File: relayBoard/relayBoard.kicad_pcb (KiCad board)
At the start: 4 copper layers, 181.6 x 270.5 mm, 233 parts, among them J1 Conn_01x10, J10 Conn_02x07_Odd_Even, J11 Conn_01x10, J12 Conn_01x10, J13 Conn_01x10, J14 DB50_CON, J2 Conn_01x10, J3 Conn_01x01, J4 Conn_01x01, J5 Conn_01x01, J6 Conn_01x01, J7 Conn_01x01, J8 Conn_01x01, J9 Conn_02x07_Odd_Even, K1 G6S-2, K10 G6S-2, K11 G6S-2, K12 G6S-2, K13 G6S-2, K14 G6S-2, K15 G6S-2, K16 G6S-2, K17 G6S-2, K18 G6S-2, K19 G6S-2, K2 G6S-2, K20 G6S-2, K21 G6S-2, K22 G6S-2, K23 G6S-2, K24 G6S-2, K25 G6S-2, K26 G6S-2, K27 G6S-2, K28 G6S-2, K29 G6S-2, K3 G6S-2, K30 G6S-2, K31 G6S-2, K32 G6S-2, K33 G6S-2, K34 G6S-2, K35 G6S-2, K36 G6S-2, K37 G6S-2, K38 G6S-2, K39 G6S-2, K4 G6S-2, K40 G6S-2, K5 G6S-2, K6 G6S-2, K7 G6S-2, K8 G6S-2, K9 G6S-2, Q1 Q_NMOS_DGS, Q10 Q_NMOS_DGS, Q11 Q_NMOS_DGS, Q12 Q_NMOS_DGS, Q13 Q_NMOS_DGS, Q14 Q_NMOS_DGS, Q15 Q_NMOS_DGS, Q16 Q_NMOS_DGS, Q17 Q_NMOS_DGS, Q18 Q_NMOS_DGS, Q19 Q_NMOS_DGS, Q2 Q_NMOS_DGS, Q20 Q_NMOS_DGS, Q21 Q_NMOS_DGS, Q22 Q_NMOS_DGS, Q23 Q_NMOS_DGS, Q24 Q_NMOS_DGS, Q25 Q_NMOS_DGS, Q26 Q_NMOS_DGS, Q27 Q_NMOS_DGS, Q28 Q_NMOS_DGS, Q29 Q_NMOS_DGS, Q3 Q_NMOS_DGS, Q30 Q_NMOS_DGS, Q31 Q_NMOS_DGS, Q32 Q_NMOS_DGS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

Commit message: First pass layout finished
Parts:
- removed JP1, JP2, JP3: Jumper_3_Bridged12, Connector_PinHeader_2.00mm:PinHeader_1x03_P2.00mm_Vertical
- removed JP4: Jumper_2_Bridged, Connector_PinHeader_2.54mm:PinHeader_1x02_P2.54mm_Vertical
- added C10: C, Resistor_SMD:R_0603_1608Metric, F.Cu at (131.3, 85.0)
- added C11: C, Resistor_SMD:R_0603_1608Metric, F.Cu at (131.3, 75.0)
- added C12: C, Resistor_SMD:R_0603_1608Metric, F.Cu at (131.3, 65.0)
- added C13: C, Resistor_SMD:R_0603_1608Metric, F.Cu at (131.3, 55.0)
- added C14: C, Resistor_SMD:R_0603_1608Metric, F.Cu at (131.3, 45.0)
- added C15: C, Resistor_SMD:R_0603_1608Metric, F.Cu at (131.3, 35.0)
- added C16: C, Resistor_SMD:R_0603_1608Metric, F.Cu at (131.3, 25.0)
- added C17: C, Resistor_SMD:R_0603_1608Metric, F.Cu at (131.3, 15.0)
- added C18: C, Resistor_SMD:R_0603_1608Metric, F.Cu at (131.3, 4.98)
- added C19: C, Resistor_SMD:R_0603_1608Metric, F.Cu at (131.3, -5.02)
- added C20: C, Resistor_SMD:R_0603_1608Metric, F.Cu at (131.3, -15.0)
- added C21: C, Resistor_SMD:R_0603_1608Metric, F.Cu at (131.3, -25.0)
- added C22: C, Resistor_SMD:R_0603_1608Metric, F.Cu at (81.3, 175.0)
- added C23: C, Resistor_SMD:R_0603_1608Metric, F.Cu at (81.3, 165.0)
- added C24: C, Resistor_SMD:R_0603_1608Metric, F.Cu at (81.3, 155.0)
- added C25: C, Resistor_SMD:R_0603_1608Metric, F.Cu at (81.3, 145.0)
- added C26: C, Resistor_SMD:R_0603_1608Metric, F.Cu at (81.3, 135.0)
- added C27: C, Resistor_SMD:R_0603_1608Metric, F.Cu at (81.3, 125.0)
- added C28: C, Resistor_SMD:R_0603_1608Metric, F.Cu at (81.3, 115.0)
- added C29: C, Resistor_SMD:R_0603_1608Metric, F.Cu at (81.3, 105.0)
- added C30: C, Resistor_SMD:R_0603_1608Metric, F.Cu at (81.3, 95.0)
- added C31: C, Resistor_SMD:R_0603_1608Metric, F.Cu at (81.3, 85.0)
- added C32: C, Resistor_SMD:R_0603_1608Metric, F.Cu at (81.3, 75.0)
- added C33: C, Resistor_SMD:R_0603_1608Metric, F.Cu at (81.3, 65.0)
- added C34: C, Resistor_SMD:R_0603_1608Metric, F.Cu at (81.3, 55.0)
- added C35: C, Resistor_SMD:R_0603_1608Metric, F.Cu at (81.3, 45.0)
- added C36: C, Resistor_SMD:R_0603_1608Metric, F.Cu at (81.3, 35.0)
- added C37: C, Resistor_SMD:R_0603_1608Metric, F.Cu at (81.3, 25.0)
- added C38: C, Resistor_SMD:R_0603_1608Metric, F.Cu at (81.3, 15.0)
- added C39: C, Resistor_SMD:R_0603_1608Metric, F.Cu at (81.3, 4.98)
- added C4: C, Resistor_SMD:R_0603_1608Metric, F.Cu at (131.3, 145.0)
- added C40: C, Resistor_SMD:R_0603_1608Metric, F.Cu at (81.3, -5.02)
- added C41: C, Resistor_SMD:R_0603_1608Metric, F.Cu at (81.3, -15.0)
- added C42: C, Resistor_SMD:R_0603_1608Metric, F.Cu at (81.3, -25.0)
- added C43: C, Resistor_SMD:R_0603_1608Metric, F.Cu at (148.8, 70.4)
- added C44: C, Resistor_SMD:R_0603_1608Metric, F.Cu at (95.2, 81.3)
- added C45: C, Resistor_SMD:R_0603_1608Metric, F.Cu at (93.0, 53.8)
- added C46: C, Resistor_SMD:R_0603_1608Metric, F.Cu at (209.8, 144.8)
- added C47: 10u, Resistor_SMD:R_0603_1608Metric, F.Cu at (19.1, 104.1)
- added C48: 10u, Resistor_SMD:R_0603_1608Metric, F.Cu at (26.4, 98.8)
- added C49: C, Resistor_SMD:R_0603_1608Metric, F.Cu at (133.9, -42.2)
- added C5: C, Resistor_SMD:R_0603_1608Metric, F.Cu at (131.3, 135.0)
- added C50: 10u, Resistor_SMD:R_0603_1608Metric, F.Cu at (90.7, -37.1)
- added C51: 1u, Resistor_SMD:R_0603_1608Metric, F.Cu at (95.5, -34.3)
- added C52: 470p, Resistor_SMD:R_0603_1608Metric, F.Cu at (105.9, -45.7)
- added C53: 220u, Resistor_SMD:R_1210_3225Metric, F.Cu at (145.5, -38.6)
- added C6: C, Resistor_SMD:R_0603_1608Metric, F.Cu at (131.3, 125.0)
- added C7: C, Resistor_SMD:R_0603_1608Metric, F.Cu at (131.3, 115.0)
- added C8: C, Resistor_SMD:R_0603_1608Metric, F.Cu at (131.3, 105.0)
- added C9: C, Resistor_SMD:R_0603_1608Metric, F.Cu at (131.3, 95.0)
- added D100: LED, Resistor_SMD:R_0805_2012Metric, F.Cu at (81.1, 59.3)
- added D101: D_Zener, Diode_SMD:D_0805_2012Metric, F.Cu at (76.5, 59.3)
- added D102: D_Zener, Diode_SMD:D_0805_2012Metric, F.Cu at (86.7, 54.5)
- added D103: LED, Resistor_SMD:R_0805_2012Metric, F.Cu at (81.1, 49.3)
- added D104: D_Zener, Diode_SMD:D_0805_2012Metric, F.Cu at (76.5, 49.3)
- added D105: D_Zener, Diode_SMD:D_0805_2012Metric, F.Cu at (86.7, 44.5)
- added D106: LED, Resistor_SMD:R_0805_2012Metric, F.Cu at (81.1, 39.3)
- added D107: D_Zener, Diode_SMD:D_0805_2012Metric, F.Cu at (76.5, 39.3)
- added D108: D_Zener, Diode_SMD:D_0805_2012Metric, F.Cu at (86.7, 34.5)
- added D109: LED, Resistor_SMD:R_0805_2012Metric, F.Cu at (81.1, 29.3)
- added D110: D_Zener, Diode_SMD:D_0805_2012Metric, F.Cu at (76.5, 29.3)
- added D111: D_Zener, Diode_SMD:D_0805_2012Metric, F.Cu at (86.7, 24.5)
- added D112: LED, Resistor_SMD:R_0805_2012Metric, F.Cu at (81.1, 19.3)
- added D113: D_Zener, Diode_SMD:D_0805_2012Metric, F.Cu at (76.5, 19.3)
- added D114: D_Zener, Diode_SMD:D_0805_2012Metric, F.Cu at (86.7, 14.5)
- added D115: LED, Resistor_SMD:R_0805_2012Metric, F.Cu at (81.1, 9.32)
- added D116: D_Zener, Diode_SMD:D_0805_2012Metric, F.Cu at (76.5, 9.32)
- added D117: D_Zener, Diode_SMD:D_0805_2012Metric, F.Cu at (86.7, 4.50)
- added D118: LED, Resistor_SMD:R_0805_2012Metric, F.Cu at (81.1, -0.68)
- added D119: D_Zener, Diode_SMD:D_0805_2012Metric, F.Cu at (76.5, -0.68)
- added D120: D_Zener, Diode_SMD:D_0805_2012Metric, F.Cu at (86.7, -5.50)
- added D121: LED, Resistor_SMD:R_0805_2012Metric, F.Cu at (81.1, -10.7)
- added D122: D_Zener, Diode_SMD:D_0805_2012Metric, F.Cu at (76.5, -10.7)
- added D123: D_Zener, Diode_SMD:D_0805_2012Metric, F.Cu at (86.7, -15.5)
- added D124: LED, Resistor_SMD:R_0805_2012Metric, F.Cu at (81.1, -20.7)
- added D125: D_Zener, Diode_SMD:D_0805_2012Metric, F.Cu at (76.5, -20.7)
- added D126: D_Zener, Diode_SMD:D_0805_2012Metric, F.Cu at (86.7, -25.5)
- added D127: LED, Resistor_SMD:R_0805_2012Metric, F.Cu at (200.4, 176.8)
- added D128: LED, Resistor_SMD:R_0805_2012Metric, F.Cu at (200.4, 166.8)
- added D129: LED, Resistor_SMD:R_0805_2012Metric, F.Cu at (200.4, 156.8)
- added D130: LED, Resistor_SMD:R_0805_2012Metric, F.Cu at (200.4, 146.8)
- added D131: LED, Resistor_SMD:R_0805_2012Metric, F.Cu at (200.4, 136.8)
- added D132: LED, Resistor_SMD:R_0805_2012Metric, F.Cu at (200.4, 126.8)
- added D133: LED, Resistor_SMD:R_0805_2012Metric, F.Cu at (200.4, 116.8)
- added D134: LED, Resistor_SMD:R_0805_2012Metric, F.Cu at (200.4, 106.8)
- added D135: LED, Resistor_SMD:R_0805_2012Metric, F.Cu at (200.4, 96.8)
- added D136: LED, Resistor_SMD:R_0805_2012Metric, F.Cu at (200.4, 86.8)
- added D137: LED, Resistor_SMD:R_0805_2012Metric, F.Cu at (200.4, 76.8)
- added D138: LED, Resistor_SMD:R_0805_2012Metric, F.Cu at (200.4, 66.8)
- added D139: LED, Resistor_SMD:R_0805_2012Metric, F.Cu at (200.4, 56.8)
- added D140: LED, Resistor_SMD:R_0805_2012Metric, F.Cu at (200.4, 46.8)
- added D141: LED, Resistor_SMD:R_0805_2012Metric, F.Cu at (200.4, 36.8)
- added D142: LED, Resistor_SMD:R_0805_2012Metric, F.Cu at (200.4, 26.8)
- added D143: LED, Resistor_SMD:R_0805_2012Metric, F.Cu at (200.4, 16.8)
- added D144: LED, Resistor_SMD:R_0805_2012Metric, F.Cu at (200.4, 6.78)
- added D145: LED, Resistor_SMD:R_0805_2012Metric, F.Cu at (200.4, -3.22)
- added D146: LED, Resistor_SMD:R_0805_2012Metric, F.Cu at (200.4, -13.2)
- added D147: LED, Resistor_SMD:R_0805_2012Metric, F.Cu at (200.4, -23.2)
- added D148: CMZ5934B, Diode_SMD:D_SMA, F.Cu at (96.5, -49.0)
- added D149: DFLS1100, Diode_SMD:D_PowerDI-123, F.Cu at (105.9, -49.0)
- added D150: D, Diode_SMD:D_0805_2012Metric, F.Cu at (149.4, -29.5)
- added D151: PDS360, Diode_SMD:D_PowerDI-5, F.Cu at (130.4, -45.5)
- added D41: D_Zener, Diode_SMD:D_0805_2012Metric, F.Cu at (126.5, 49.3)
- added D42: D_Zener, Diode_SMD:D_0805_2012Metric, F.Cu at (136.7, 44.5)
- added D43: LED, Resistor_SMD:R_0805_2012Metric, F.Cu at (131.1, 39.3)
- added D44: D_Zener, Diode_SMD:D_0805_2012Metric, F.Cu at (126.5, 39.3)
- added D45: D_Zener, Diode_SMD:D_0805_2012Metric, F.Cu at (136.7, 34.5)
- added D46: LED, Resistor_SMD:R_0805_2012Metric, F.Cu at (131.1, 29.3)
- added D47: D_Zener, Diode_SMD:D_0805_2012Metric, F.Cu at (126.5, 29.3)
- added D48: D_Zener, Diode_SMD:D_0805_2012Metric, F.Cu at (136.7, 24.5)
- added D49: LED, Resistor_SMD:R_0805_2012Metric, F.Cu at (131.1, 19.3)
- added D50: D_Zener, Diode_SMD:D_0805_2012Metric, F.Cu at (126.5, 19.3)
- added D51: D_Zener, Diode_SMD:D_0805_2012Metric, F.Cu at (136.7, 14.5)
- added D52: LED, Resistor_SMD:R_0805_2012Metric, F.Cu at (131.1, 9.32)
- added D53: D_Zener, Diode_SMD:D_0805_2012Metric, F.Cu at (126.5, 9.32)
- added D54: D_Zener, Diode_SMD:D_0805_2012Metric, F.Cu at (136.7, 4.50)
- added D55: LED, Resistor_SMD:R_0805_2012Metric, F.Cu at (131.1, -0.68)
- added D56: D_Zener, Diode_SMD:D_0805_2012Metric, F.Cu at (126.5, -0.68)
- added D57: D_Zener, Diode_SMD:D_0805_2012Metric, F.Cu at (136.7, -5.50)
- added D58: LED, Resistor_SMD:R_0805_2012Metric, F.Cu at (131.1, -10.7)
- added D59: D_Zener, Diode_SMD:D_0805_2012Metric, F.Cu at (126.5, -10.7)
- added D60: D_Zener, Diode_SMD:D_0805_2012Metric, F.Cu at (136.7, -15.5)
- added D61: LED, Resistor_SMD:R_0805_2012Metric, F.Cu at (131.1, -20.7)
- added D62: D_Zener, Diode_SMD:D_0805_2012Metric, F.Cu at (126.5, -20.7)
- added D63: D_Zener, Diode_SMD:D_0805_2012Metric, F.Cu at (136.7, -25.5)
- added D64: LED, Resistor_SMD:R_0805_2012Metric, F.Cu at (81.1, 179.3)
- added D65: D_Zener, Diode_SMD:D_0805_2012Metric, F.Cu at (76.5, 179.3)
- added D66: D_Zener, Diode_SMD:D_0805_2012Metric, F.Cu at (86.7, 174.5)
- added D67: LED, Resistor_SMD:R_0805_2012Metric, F.Cu at (81.1, 169.3)
- added D68: D_Zener, Diode_SMD:D_0805_2012Metric, F.Cu at (76.5, 169.3)
- added D69: D_Zener, Diode_SMD:D_0805_2012Metric, F.Cu at (86.7, 164.5)
- added D70: LED, Resistor_SMD:R_0805_2012Metric, F.Cu at (81.1, 159.3)
- added D71: D_Zener, Diode_SMD:D_0805_2012Metric, F.Cu at (76.5, 159.3)
- added D72: D_Zener, Diode_SMD:D_0805_2012Metric, F.Cu at (86.7, 154.5)
- added D73: LED, Resistor_SMD:R_0805_2012Metric, F.Cu at (81.1, 149.3)
- added D74: D_Zener, Diode_SMD:D_0805_2012Metric, F.Cu at (76.5, 149.3)
- added D75: D_Zener, Diode_SMD:D_0805_2012Metric, F.Cu at (86.7, 144.5)
- added D76: LED, Resistor_SMD:R_0805_2012Metric, F.Cu at (81.1, 139.3)
- added D77: D_Zener, Diode_SMD:D_0805_2012Metric, F.Cu at (76.5, 139.3)
- added D78: D_Zener, Diode_SMD:D_0805_2012Metric, F.Cu at (86.7, 134.5)
- added D79: LED, Resistor_SMD:R_0805_2012Metric, F.Cu at (81.1, 129.3)
- added D80: D_Zener, Diode_SMD:D_0805_2012Metric, F.Cu at (76.5, 129.3)
- added D81: D_Zener, Diode_SMD:D_0805_2012Metric, F.Cu at (86.7, 124.5)
- added D82: LED, Resistor_SMD:R_0805_2012Metric, F.Cu at (81.1, 119.3)
- added D83: D_Zener, Diode_SMD:D_0805_2012Metric, F.Cu at (76.5, 119.3)
- added D84: D_Zener, Diode_SMD:D_0805_2012Metric, F.Cu at (86.7, 114.5)
- added D85: LED, Resistor_SMD:R_0805_2012Metric, F.Cu at (81.1, 109.3)
- added D86: D_Zener, Diode_SMD:D_0805_2012Metric, F.Cu at (76.5, 109.3)
- added D87: D_Zener, Diode_SMD:D_0805_2012Metric, F.Cu at (86.7, 104.5)
- added D88: LED, Resistor_SMD:R_0805_2012Metric, F.Cu at (81.1, 99.3)
- added D89: D_Zener, Diode_SMD:D_0805_2012Metric, F.Cu at (76.5, 99.3)
- added D90: D_Zener, Diode_SMD:D_0805_2012Metric, F.Cu at (86.7, 94.5)
- added D91: LED, Resistor_SMD:R_0805_2012Metric, F.Cu at (81.1, 89.3)
- added D92: D_Zener, Diode_SMD:D_0805_2012Metric, F.Cu at (76.5, 89.3)
- added D93: D_Zener, Diode_SMD:D_0805_2012Metric, F.Cu at (86.7, 84.5)
- added D94: LED, Resistor_SMD:R_0805_2012Metric, F.Cu at (81.1, 79.3)
- added D95: D_Zener, Diode_SMD:D_0805_2012Metric, F.Cu at (76.5, 79.3)
- added D96: D_Zener, Diode_SMD:D_0805_2012Metric, F.Cu at (86.7, 74.5)
- added D97: LED, Resistor_SMD:R_0805_2012Metric, F.Cu at (81.1, 69.3)
- added D98: D_Zener, Diode_SMD:D_0805_2012Metric, F.Cu at (76.5, 69.3)
- added D99: D_Zener, Diode_SMD:D_0805_2012Metric, F.Cu at (86.7, 64.5)
- added IC1: ADUM1251, ADUM1251:SO08, F.Cu at (37.6, 155.2)
- added K41: G6S-2, Relay_THT:Relay_DPDT_Omron_G6SK-2, F.Cu at (72.4, -15.0)
- added K42: G6S-2, Relay_THT:Relay_DPDT_Omron_G6SK-2, F.Cu at (72.4, -25.0)
- added K43: CPC1708J, TO381P2016X515X2916-4:TO381P2016X515X2916-4, F.Cu at (172.4, 177.5)
- added K44: CPC1708J, TO381P2016X515X2916-4:TO381P2016X515X2916-4, F.Cu at (172.4, 167.5)
- added K45: CPC1708J, TO381P2016X515X2916-4:TO381P2016X515X2916-4, F.Cu at (172.4, 157.5)
- added K46: CPC1708J, TO381P2016X515X2916-4:TO381P2016X515X2916-4, F.Cu at (172.4, 147.5)
- added K47: CPC1708J, TO381P2016X515X2916-4:TO381P2016X515X2916-4, F.Cu at (172.4, 137.5)
- added K48: CPC1708J, TO381P2016X515X2916-4:TO381P2016X515X2916-4, F.Cu at (172.4, 127.5)
- added K49: CPC1708J, TO381P2016X515X2916-4:TO381P2016X515X2916-4, F.Cu at (172.4, 117.5)
- added K50: CPC1708J, TO381P2016X515X2916-4:TO381P2016X515X2916-4, F.Cu at (172.4, 107.5)
- added K51: CPC1708J, TO381P2016X515X2916-4:TO381P2016X515X2916-4, F.Cu at (172.4, 97.5)
- added K52: CPC1708J, TO381P2016X515X2916-4:TO381P2016X515X2916-4, F.Cu at (172.4, 87.5)
- added K53: CPC1708J, TO381P2016X515X2916-4:TO381P2016X515X2916-4, F.Cu at (172.4, 77.5)
- added K54: CPC1708J, TO381P2016X515X2916-4:TO381P2016X515X2916-4, F.Cu at (172.4, 67.5)
- added K55: CPC1708J, TO381P2016X515X2916-4:TO381P2016X515X2916-4, F.Cu at (172.4, 57.5)
- added K56: CPC1708J, TO381P2016X515X2916-4:TO381P2016X515X2916-4, F.Cu at (172.4, 47.5)
- added K57: CPC1708J, TO381P2016X515X2916-4:TO381P2016X515X2916-4, F.Cu at (172.4, 37.5)
- added K58: CPC1708J, TO381P2016X515X2916-4:TO381P2016X515X2916-4, F.Cu at (172.4, 27.5)
- added K59: CPC1708J, TO381P2016X515X2916-4:TO381P2016X515X2916-4, F.Cu at (172.4, 17.5)
- added K60: CPC1708J, TO381P2016X515X2916-4:TO381P2016X515X2916-4, F.Cu at (172.4, 7.51)
- added K61: CPC1708J, TO381P2016X515X2916-4:TO381P2016X515X2916-4, F.Cu at (172.4, -2.49)
- added K62: CPC1708J, TO381P2016X515X2916-4:TO381P2016X515X2916-4, F.Cu at (172.4, -12.5)
- added K63: CPC1708J, TO381P2016X515X2916-4:TO381P2016X515X2916-4, F.Cu at (172.4, -22.5)
- added Q41: Q_NMOS_DGS, Package_TO_SOT_SMD:SOT-23, F.Cu at (84.1, -11.7)
- added Q42: Q_NMOS_DGS, Package_TO_SOT_SMD:SOT-23, F.Cu at (84.1, -21.7)
- added Q43: Q_NJFET_GSD, Package_TO_SOT_SMD:Infineon_PG-TO-220-7Lead_TabPin8, F.Cu at (160.3, -33.7)
- added R100: 0, Resistor_SMD:R_0603_1608Metric, F.Cu at (76.5, 55.0)
- added R101: 1k, Resistor_SMD:R_0603_1608Metric, F.Cu at (78.3, 55.0)
- added R102: 100, Resistor_SMD:R_0603_1608Metric, F.Cu at (88.2, 58.6)
- added R103: 0, Resistor_SMD:R_0603_1608Metric, F.Cu at (76.5, 45.0)
- added R104: 1k, Resistor_SMD:R_0603_1608Metric, F.Cu at (78.3, 45.0)
- added R105: 100, Resistor_SMD:R_0603_1608Metric, F.Cu at (88.2, 48.6)
- added R106: 0, Resistor_SMD:R_0603_1608Metric, F.Cu at (76.5, 35.0)
- added R107: 1k, Resistor_SMD:R_0603_1608Metric, F.Cu at (78.3, 35.0)
- added R108: 100, Resistor_SMD:R_0603_1608Metric, F.Cu at (88.2, 38.6)
- added R109: 0, Resistor_SMD:R_0603_1608Metric, F.Cu at (76.5, 25.0)
- added R110: 1k, Resistor_SMD:R_0603_1608Metric, F.Cu at (78.3, 25.0)
- added R111: 100, Resistor_SMD:R_0603_1608Metric, F.Cu at (88.2, 28.6)
- added R112: 0, Resistor_SMD:R_0603_1608Metric, F.Cu at (76.5, 15.0)
- added R113: 1k, Resistor_SMD:R_0603_1608Metric, F.Cu at (78.3, 15.0)
- added R114: 100, Resistor_SMD:R_0603_1608Metric, F.Cu at (88.2, 18.6)
- added R115: 0, Resistor_SMD:R_0603_1608Metric, F.Cu at (76.5, 5.01)
- added R116: 1k, Resistor_SMD:R_0603_1608Metric, F.Cu at (78.3, 5.01)
- added R117: 100, Resistor_SMD:R_0603_1608Metric, F.Cu at (88.2, 8.56)
- added R118: 0, Resistor_SMD:R_0603_1608Metric, F.Cu at (76.5, -4.99)
- added R119: 1k, Resistor_SMD:R_0603_1608Metric, F.Cu at (78.3, -4.99)
- added R120: 100, Resistor_SMD:R_0603_1608Metric, F.Cu at (88.2, -1.44)
- added R121: 0, Resistor_SMD:R_0603_1608Metric, F.Cu at (76.5, -15.0)
- added R122: 1k, Resistor_SMD:R_0603_1608Metric, F.Cu at (78.3, -15.0)
- added R123: 100, Resistor_SMD:R_0603_1608Metric, F.Cu at (88.2, -11.4)
- added R124: 0, Resistor_SMD:R_0603_1608Metric, F.Cu at (76.5, -25.0)
- added R125: 1k, Resistor_SMD:R_0603_1608Metric, F.Cu at (78.3, -25.0)
- added R126: 100, Resistor_SMD:R_0603_1608Metric, F.Cu at (88.2, -21.4)
- added R127: 1k, Resistor_SMD:R_0603_1608Metric, F.Cu at (197.4, 176.8)
- added R128: 1k, Resistor_SMD:R_0603_1608Metric, F.Cu at (193.0, 176.8)
- added R129: 1k, Resistor_SMD:R_0603_1608Metric, F.Cu at (197.4, 166.8)
- added R130: 1k, Resistor_SMD:R_0603_1608Metric, F.Cu at (193.0, 166.8)
- added R131: 1k, Resistor_SMD:R_0603_1608Metric, F.Cu at (197.4, 156.8)
- added R132: 1k, Resistor_SMD:R_0603_1608Metric, F.Cu at (193.0, 156.8)
- added R133: 1k, Resistor_SMD:R_0603_1608Metric, F.Cu at (197.4, 146.8)
- added R134: 1k, Resistor_SMD:R_0603_1608Metric, F.Cu at (193.0, 146.8)
- added R135: 1k, Resistor_SMD:R_0603_1608Metric, F.Cu at (197.4, 136.8)
- added R136: 1k, Resistor_SMD:R_0603_1608Metric, F.Cu at (193.0, 136.8)
- added R137: 1k, Resistor_SMD:R_0603_1608Metric, F.Cu at (197.4, 126.8)
- added R138: 1k, Resistor_SMD:R_0603_1608Metric, F.Cu at (193.0, 126.8)
- added R139: 1k, Resistor_SMD:R_0603_1608Metric, F.Cu at (197.4, 116.8)
- added R140: 1k, Resistor_SMD:R_0603_1608Metric, F.Cu at (193.0, 116.8)
- added R141: 1k, Resistor_SMD:R_0603_1608Metric, F.Cu at (197.4, 106.8)
- added R142: 1k, Resistor_SMD:R_0603_1608Metric, F.Cu at (193.0, 106.8)
- added R143: 1k, Resistor_SMD:R_0603_1608Metric, F.Cu at (197.4, 96.8)
- added R144: 1k, Resistor_SMD:R_0603_1608Metric, F.Cu at (193.0, 96.8)
- added R145: 1k, Resistor_SMD:R_0603_1608Metric, F.Cu at (197.4, 86.8)
- added R146: 1k, Resistor_SMD:R_0603_1608Metric, F.Cu at (193.0, 86.8)
- added R147: 1k, Resistor_SMD:R_0603_1608Metric, F.Cu at (197.4, 76.8)
- added R148: 1k, Resistor_SMD:R_0603_1608Metric, F.Cu at (193.0, 76.8)
- added R149: 1k, Resistor_SMD:R_0603_1608Metric, F.Cu at (197.4, 66.8)
- added R150: 1k, Resistor_SMD:R_0603_1608Metric, F.Cu at (193.0, 66.8)
- added R151: 1k, Resistor_SMD:R_0603_1608Metric, F.Cu at (197.4, 56.8)
- added R152: 1k, Resistor_SMD:R_0603_1608Metric, F.Cu at (193.0, 56.8)
- added R153: 1k, Resistor_SMD:R_0603_1608Metric, F.Cu at (197.4, 46.8)
- added R154: 1k, Resistor_SMD:R_0603_1608Metric, F.Cu at (193.0, 46.8)
- added R155: 1k, Resistor_SMD:R_0603_1608Metric, F.Cu at (197.4, 36.8)
- added R156: 1k, Resistor_SMD:R_0603_1608Metric, F.Cu at (193.0, 36.8)
- added R157: 1k, Resistor_SMD:R_0603_1608Metric, F.Cu at (197.4, 26.8)
- added R158: 1k, Resistor_SMD:R_0603_1608Metric, F.Cu at (193.0, 26.8)
- added R159: 1k, Resistor_SMD:R_0603_1608Metric, F.Cu at (197.4, 16.8)
- added R160: 1k, Resistor_SMD:R_0603_1608Metric, F.Cu at (193.0, 16.8)
- added R161: 1k, Resistor_SMD:R_0603_1608Metric, F.Cu at (197.4, 6.78)
- added R162: 1k, Resistor_SMD:R_0603_1608Metric, F.Cu at (193.0, 6.78)
- added R163: 1k, Resistor_SMD:R_0603_1608Metric, F.Cu at (197.4, -3.22)
- added R164: 1k, Resistor_SMD:R_0603_1608Metric, F.Cu at (193.0, -3.22)
- added R165: 1k, Resistor_SMD:R_0603_1608Metric, F.Cu at (197.4, -13.2)
- added R166: 1k, Resistor_SMD:R_0603_1608Metric, F.Cu at (193.0, -13.2)
- added R167: 1k, Resistor_SMD:R_0603_1608Metric, F.Cu at (197.4, -23.2)
- added R168: 1k, Resistor_SMD:R_0603_1608Metric, F.Cu at (193.0, -23.2)
- added R169: R, Resistor_SMD:R_0603_1608Metric, F.Cu at (19.6, 142.5)
- added R170: R, Resistor_SMD:R_0603_1608Metric, F.Cu at (22.6, 142.5)
- added R171: R, Resistor_SMD:R_0603_1608Metric, F.Cu at (49.3, 153.7)
- added R172: R, Resistor_SMD:R_0603_1608Metric, F.Cu at (46.5, 153.7)
- added R173: R, Resistor_SMD:R_0603_1608Metric, F.Cu at (101.6, -42.9)
- added R174: 121k, Resistor_SMD:R_0603_1608Metric, F.Cu at (104.1, -37.8)
- added R175: 10k, Resistor_SMD:R_0603_1608Metric, F.Cu at (99.8, -34.3)
- added R176: 39, Resistor_SMD:R_0603_1608Metric, F.Cu at (105.9, -42.9)
- added R177: R, Resistor_SMD:R_0603_1608Metric, F.Cu at (146.1, -33.8)
- added R178: R, Resistor_SMD:R_0603_1608Metric, F.Cu at (150.4, -33.5)
- added R86: 1k, Resistor_SMD:R_0603_1608Metric, F.Cu at (78.3, 105.0)
- added R87: 100, Resistor_SMD:R_0603_1608Metric, F.Cu at (88.2, 108.6)
- added R88: 0, Resistor_SMD:R_0603_1608Metric, F.Cu at (76.5, 95.0)
- added R89: 1k, Resistor_SMD:R_0603_1608Metric, F.Cu at (78.3, 95.0)
- added R90: 100, Resistor_SMD:R_0603_1608Metric, F.Cu at (88.2, 98.6)
- added R91: 0, Resistor_SMD:R_0603_1608Metric, F.Cu at (76.5, 85.0)
- added R92: 1k, Resistor_SMD:R_0603_1608Metric, F.Cu at (78.3, 85.0)
- added R93: 100, Resistor_SMD:R_0603_1608Metric, F.Cu at (88.2, 88.6)
- added R94: 0, Resistor_SMD:R_0603_1608Metric, F.Cu at (76.5, 75.0)
- added R95: 1k, Resistor_SMD:R_0603_1608Metric, F.Cu at (78.3, 75.0)
- added R96: 100, Resistor_SMD:R_0603_1608Metric, F.Cu at (88.2, 78.6)
- added R97: 0, Resistor_SMD:R_0603_1608Metric, F.Cu at (76.5, 65.0)
- added R98: 1k, Resistor_SMD:R_0603_1608Metric, F.Cu at (78.3, 65.0)
- added R99: 100, Resistor_SMD:R_0603_1608Metric, F.Cu at (88.2, 68.6)
- added T1: 750313457, 750313442:EP10_SMD_H_8PIN_(6052), F.Cu at (118.6, -37.8)
- added U2: PCA9555APW,118, PCA9555APW_118:SOP65P640X110-24N, F.Cu at (98.8, 88.6)
- added U3: PCA9555APW,118, PCA9555APW_118:SOP65P640X110-24N, F.Cu at (98.8, 56.6)
- added U4: PCA9555APW,118, PCA9555APW_118:SOP65P640X110-24N, F.Cu at (214.1, 150.4)
- added U5: LT1117-5.0, Package_TO_SOT_SMD:SOT-223-3_TabPin2, F.Cu at (25.1, 104.9)
- added U6: ADuM4121, Package_SO:SOIC-8_5.23x5.23mm_P1.27mm, F.Cu at (136.7, -38.4)
- added U7: LT8302, Package_SO:SO-8_3.9x4.9mm_P1.27mm, F.Cu at (98.0, -38.4)
- C1, C3: value 1u -> C; footprint Resistor_SMD:R_0603_1608Metric_Pad1.05x0.95mm_HandSolder -> Resistor_SMD:R_0603_1608Metric
- C2: value 1u -> C; footprint Resistor_SMD:R_0603_1608Metric_Pad1.05x0.95mm_HandSolder -> Resistor_SMD:R_0603_1608Metric; moved to F.Cu
- D11, D12, D14, D15, D17, D18, D2, D20, D21, D23, D24, D26, D27, D29, D3, D30, D32, D33, D35, D36, D38, D39, D5, D6, D8, D9: value LED -> D_Zener; footprint Resistor_SMD:R_0805_2012Metric -> Diode_SMD:D_0805_2012Metric
- J1, J2: value Conn_01x10 -> Conn_01x01; footprint Connector_JST:JST_EH_S10B-EH_1x10_P2.50mm_Horizontal -> Connector:Banana_Jack_1Pin
- J10, J9: value Conn_02x07_Odd_Even -> Conn_02x04_Top_Bottom; footprint Connector_PinHeader_2.00mm:PinHeader_2x07_P2.00mm_Vertical -> Connector_Molex:Molex_Micro-Fit_3.0_43045-0800_2x04_P3.00mm_Horizontal
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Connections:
- net /Channel0A/NC renamed /Channel0/NC
- net /Channel10A/NC renamed /sheet5F3D8E21/NC
- net /Channel11A/NC renamed /sheet5F3E9866/NC
- net /Channel12A/NC renamed /sheet5F3E9867/NC
- net /Channel13A/NC renamed /sheet5F3E9868/NC
- net /Channel14A/NC renamed /sheet5F3E9869/NC
- net /Channel15A/NC renamed /sheet5F3E986A/NC
- net /Channel16A/NC renamed /sheet5F3E986B/NC
- net /Channel17A/NC renamed /sheet5F3E986C/NC
- net /Channel18A/NC renamed /sheet5F3E986D/NC
- net /Channel19A/NC renamed /sheet5F3E986E/NC
- net /Channel1A/NC renamed /sheet5F3BDA77/NC
- net /Channel2A/NC renamed /sheet5F3C027D/NC
- net /Channel3A/NC renamed /sheet5F3C2351/NC
- net /Channel4A/NC renamed /sheet5F3C4950/NC
- net /Channel5A/NC renamed /sheet5F3C5DF4/NC
- net /Channel6A/NC renamed /sheet5F3C7669/NC
- net /Channel7A/NC renamed /sheet5F3C9486/NC
- net /Channel8A/NC renamed /sheet5F3CB78B/NC
- net /Channel9A/NC renamed /sheet5F3CDFA2/NC
- C1 pad 1: /5V -> Net-(C1-Pad1)
- C2 pad 1: GND -> Net-(C2-Pad1)
- C2 pad 2: /5V -> GND
- C3 pad 1: +12V -> Net-(C3-Pad1)
- D11 pad 1: Net-(D11-Pad1) -> Net-(C4-Pad1)
- D11 pad 2: Net-(D11-Pad2) -> Net-(D10-Pad1)
- D12 pad 2: Net-(D12-Pad2) -> GND
- D14 pad 1: Net-(D14-Pad1) -> Net-(C5-Pad1)
- D14 pad 2: Net-(D14-Pad2) -> Net-(D13-Pad1)
- D15 pad 2: Net-(D15-Pad2) -> GND
- D17 pad 1: Net-(D17-Pad1) -> Net-(C6-Pad1)
- D17 pad 2: Net-(D17-Pad2) -> Net-(D16-Pad1)
- D18 pad 2: Net-(D18-Pad2) -> GND
- D2 pad 1: Net-(D2-Pad1) -> Net-(C1-Pad1)
- D2 pad 2: Net-(D2-Pad2) -> Net-(D1-Pad1)
- D20 pad 1: Net-(D20-Pad1) -> Net-(C7-Pad1)
- D20 pad 2: Net-(D20-Pad2) -> Net-(D19-Pad1)
- D21 pad 2: Net-(D21-Pad2) -> GND
- D23 pad 1: Net-(D23-Pad1) -> Net-(C8-Pad1)
- D23 pad 2: Net-(D23-Pad2) -> Net-(D22-Pad1)
- D24 pad 2: Net-(D24-Pad2) -> GND
- D26 pad 1: Net-(D26-Pad1) -> Net-(C9-Pad1)
- D26 pad 2: Net-(D26-Pad2) -> Net-(D25-Pad1)
- D27 pad 2: Net-(D27-Pad2) -> GND
- D29 pad 1: Net-(D29-Pad1) -> Net-(C10-Pad1)
- D29 pad 2: Net-(D29-Pad2) -> Net-(D28-Pad1)
- D3 pad 2: Net-(D3-Pad2) -> GND
- D30 pad 2: Net-(D30-Pad2) -> GND
- D32 pad 1: Net-(D32-Pad1) -> Net-(C11-Pad1)
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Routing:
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- added copper zone on F.Cu, net +12V
- added copper zone on In1.Cu, net +12V
- added copper zone on F.Cu, net +5V
- added copper zone on In1.Cu, net +5V
- added copper zone on In2.Cu, net /INPUT_1
- added copper zone on F.Cu, net /INPUT_2
- added copper zone on In2.Cu, net /INPUT_2
- added copper zone on F.Cu, net /INPUT_2_IN
- added copper zone on F.Cu, net GND
- removed copper zone on In2.Cu, net +12V
- removed copper zone on F.Cu, net /5V
- removed copper zone on In2.Cu, net /5V
- removed copper zone on In2.Cu, net /5V_LIN
- removed copper zone on B.Cu, net GND
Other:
- board size 181.6 x 270.5 mm -> 220.7 x 245.6 mm
- board text removed: "12V"
- board text removed: "12V No 5V"
- board text removed: "5V"
- board text removed: "5V/12V"
- board text removed: "A0"
- board text removed: "A1"
- board text removed: "A2"
- board text removed: "Cell Inputs"
- board text removed: "Cells"
- board text removed: "High Voltage"
- board text removed: "Linduino 5V"
- board text removed: "No Power"
- board text removed: "Power"
- board text removed: "Relay Output"
- board text removed: "Relay Outputs"

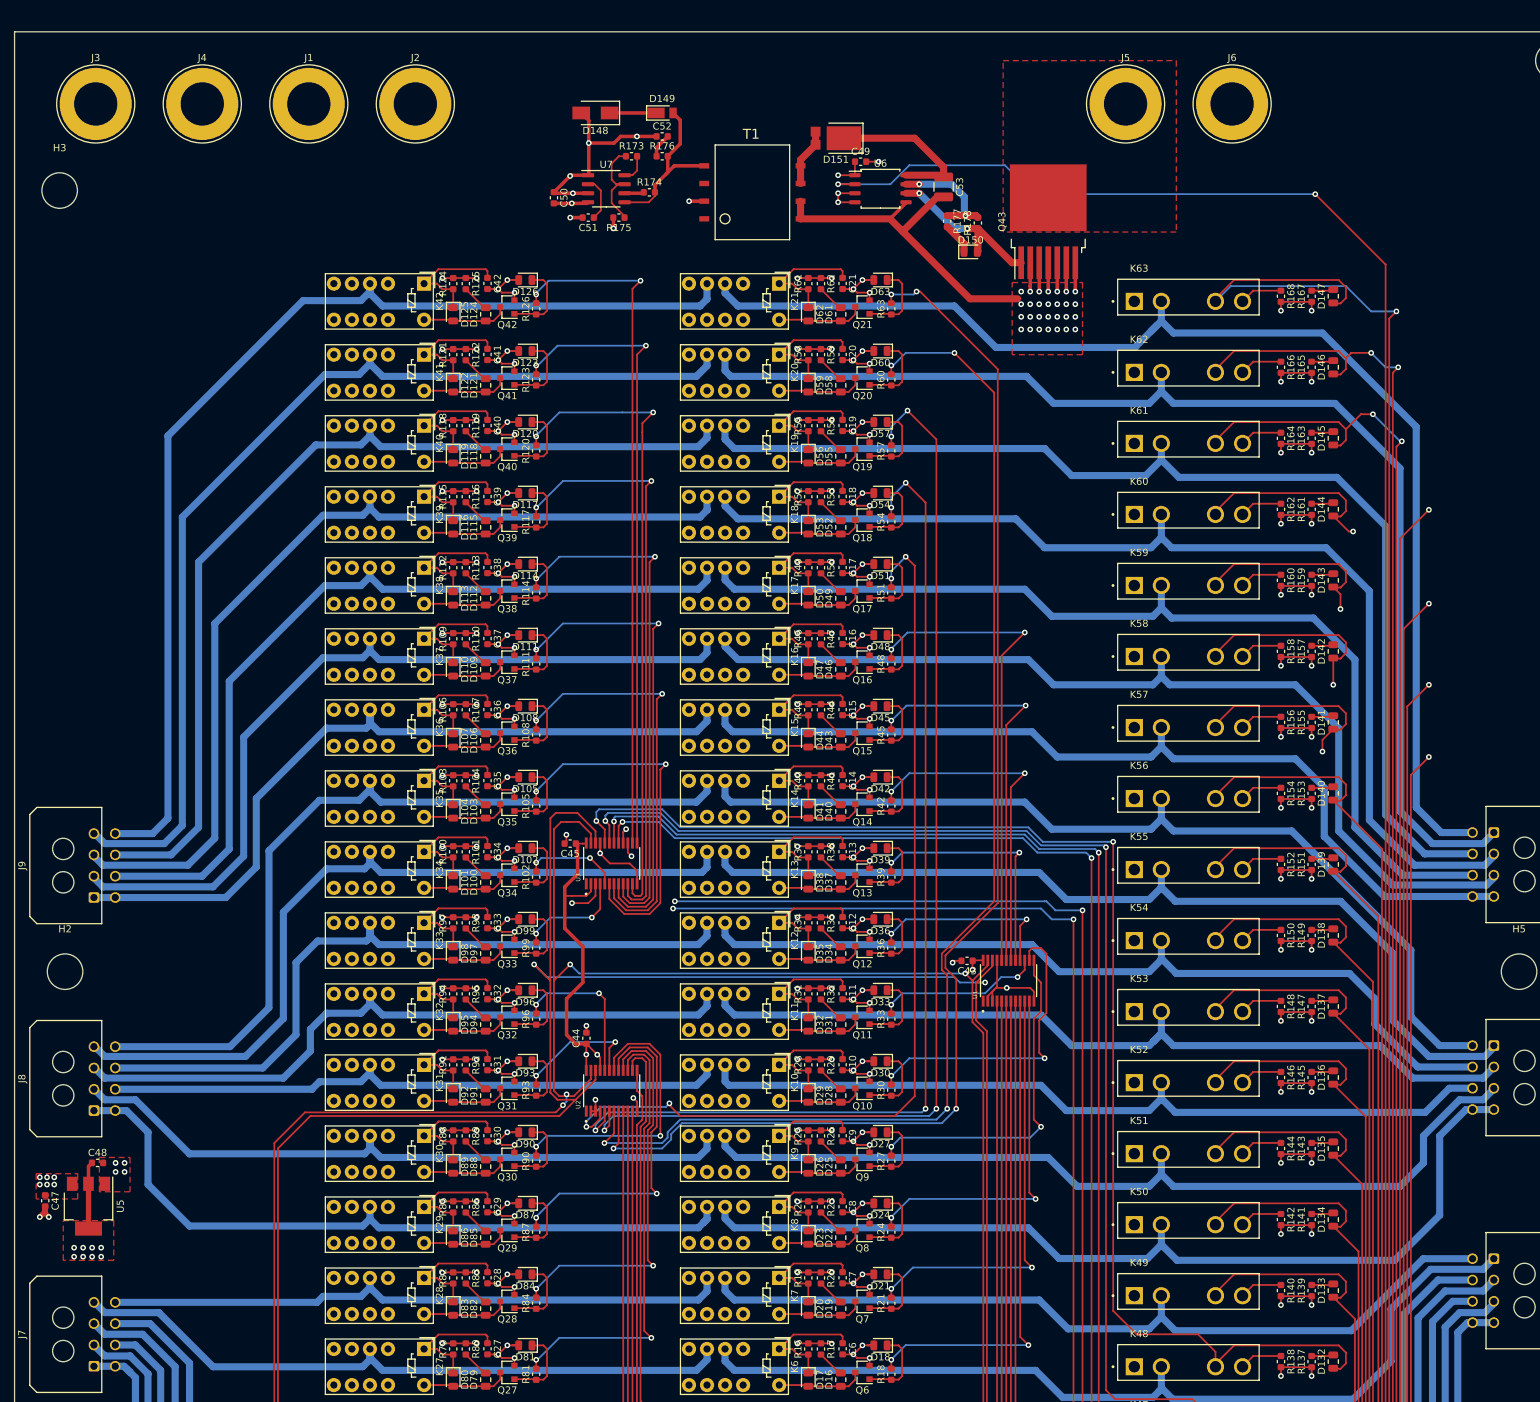
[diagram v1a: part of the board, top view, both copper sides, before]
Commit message: second pass relay board layout
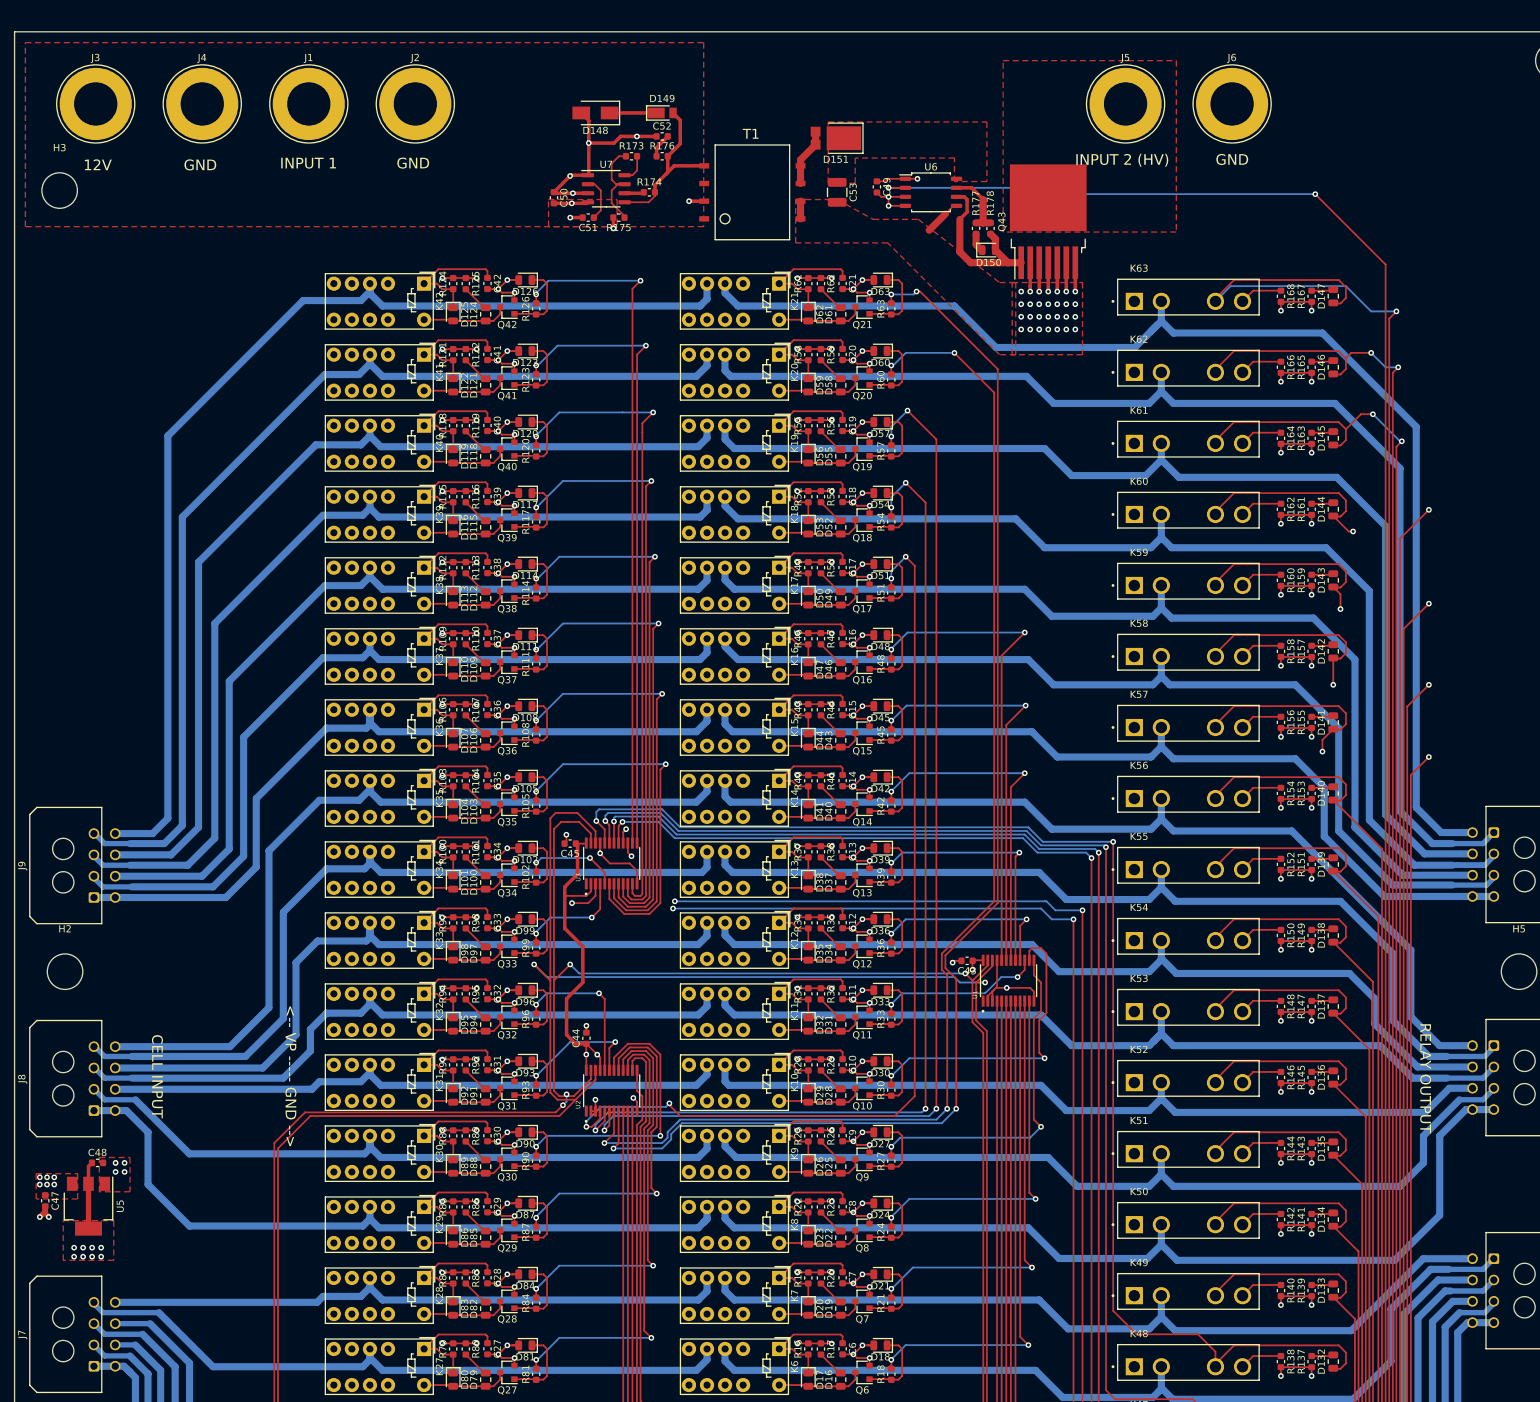
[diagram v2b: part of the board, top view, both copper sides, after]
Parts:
- moved C53 15.0 mm to (130.6, -37.8)
- moved U6 7.13 mm to (143.8, -37.8)
- moved C49 4.23 mm to (136.1, -38.6), turned to 270 degrees
- moved R177 4.19 mm to (150.1, -32.8)
- moved D150 2.55 mm to (151.9, -29.7)
- moved R178 1.93 mm to (152.1, -32.8)
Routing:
- net /INPUT_2: track 73.0 -> 32.0 mm
- net /Sheet5F711699/GATE_SUP: track 32.7 -> 0.00 mm
- net /HV_SW: track 263.8 -> 254.2 mm
- net Net-(R177-Pad1): track 16.3 -> 9.75 mm, vias 2 -> 0
- net /OUT17: track 154.7 -> 159.0 mm
- net Net-(D150-Pad1): track 4.51 -> 2.65 mm
- net +5V: track 285.7 -> 287.2 mm
- net Net-(D150-Pad2): track 24.8 -> 23.8 mm, vias 2 -> 0
- net GND: track 465.7 -> 466.1 mm, vias 150 -> 149
- added copper zone on F.Cu, net /Sheet5F711699/GATE_SUP
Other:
- board text added: "12V"
- board text added: "<-- VP ----- GND -->"
- board text added: "CELL INPUT"
- board text added: "GND"
- board text added: "INPUT 1"
- board text added: "INPUT 2 (HV)"
- board text added: "RELAY OUTPUT"

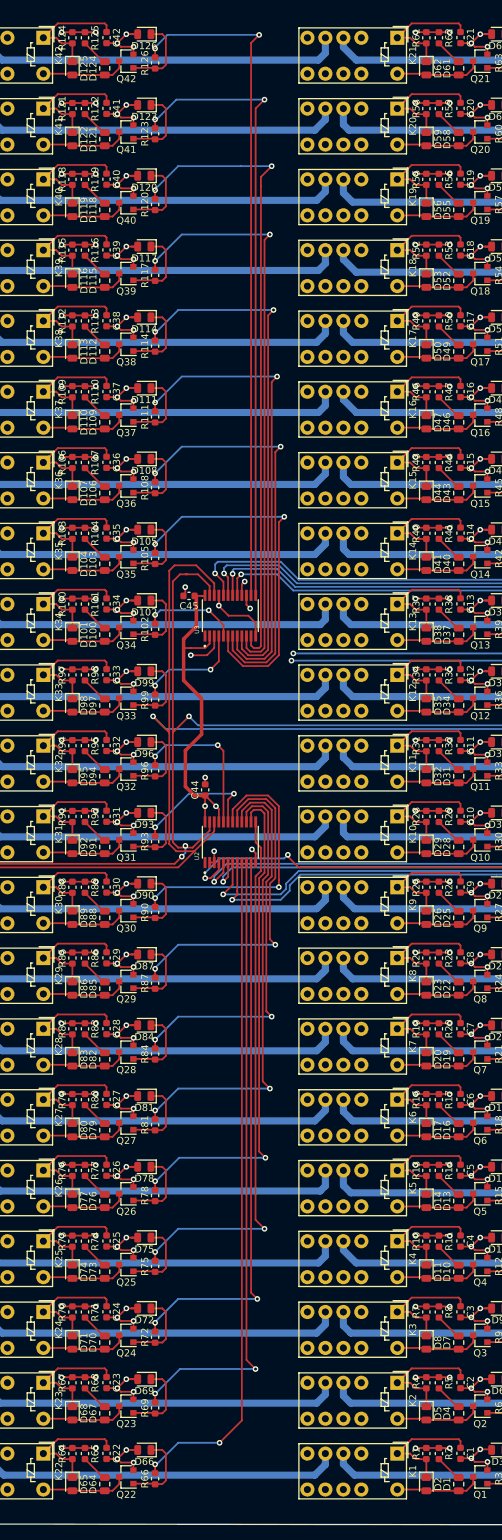
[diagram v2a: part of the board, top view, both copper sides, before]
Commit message: Third pass, fixing footprints to match JLC components
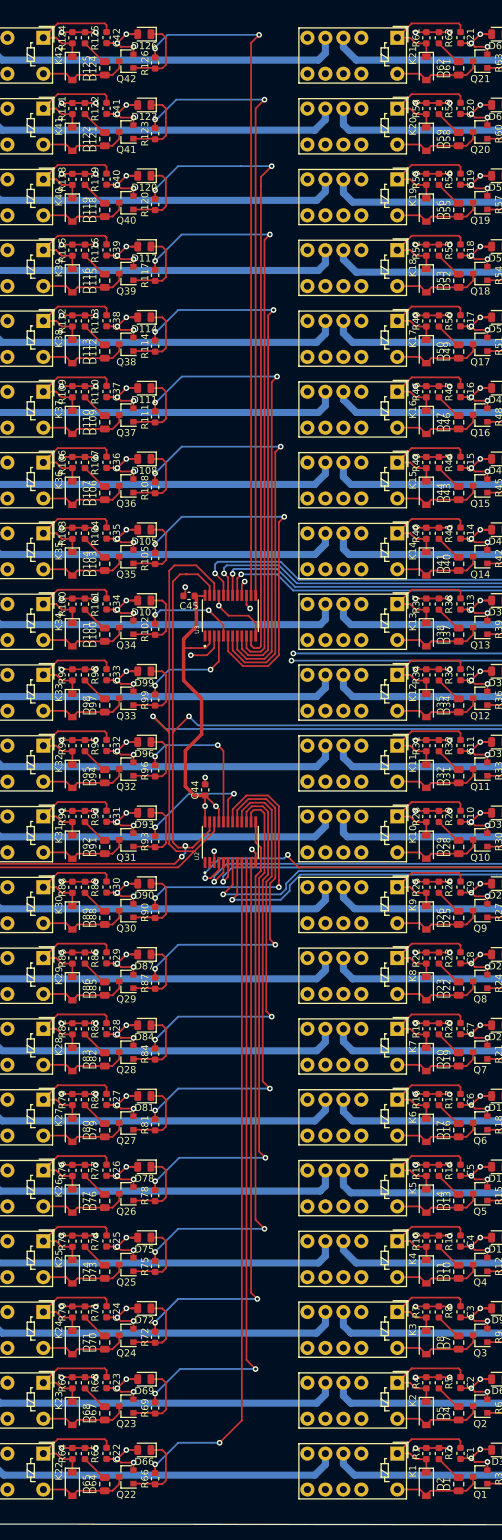
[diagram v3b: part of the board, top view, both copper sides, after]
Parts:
- C1, C10, C11, C12, C13, C14, C15, C16, C17, C18, C19, C2, C20, C21, C22, C23, C24, C25, C26, C27, C28, C29, C3, C30, C31, C32, C33, C34, C35, C36, C37, C38, C39, C4, C40, C41, C42, C5, C6, C7, C8, C9: value C -> 10n
- C43, C44, C45, C46: value C -> 100n
- C49: value C -> 1u
- D1, D10, D100, D103, D106, D109, D112, D115, D118, D121, D124, D127, D128, D129, D13, D130, D131, D132, D133, D134, D135, D136, D137, D138, D139, D140, D141, D142, D143, D144, D145, D146, D147, D16, D19, D22, D25, D28, D31, D34, D37, D4, D40, D43, D46, D49, D52, D55, D58, D61, D64, D67, D7, D70, D73, D76, D79, D82, D85, D88, D91, D94, D97: value LED -> 17-21SUYC/TR8
- D101, D104, D107, D11, D110, D113, D116, D119, D122, D125, D14, D17, D2, D20, D23, D26, D29, D32, D35, D38, D41, D44, D47, D5, D50, D53, D56, D59, D62, D65, D68, D71, D74, D77, D8, D80, D83, D86, D89, D92, D95, D98: value D_Zener -> MMSZ5245B-E3-08; footprint Diode_SMD:D_0805_2012Metric -> Diode_SMD:D_SOD-123
- K1, K10, K11, K12, K13, K14, K15, K16, K17, K18, K19, K2, K20, K21, K22, K23, K24, K25, K26, K27, K28, K29, K3, K30, K31, K32, K33, K34, K35, K36, K37, K38, K39, K4, K40, K41, K42, K5, K6, K7, K8, K9: value G6S-2 -> G6S-2 DC12
- K43, K44, K45, K46, K47, K48, K49, K50, K51, K52, K53, K54, K55, K56, K57, K58, K59, K60, K61, K62, K63: value CPC1708J -> CPC1777J
- Q1, Q10, Q11, Q12, Q13, Q14, Q15, Q16, Q17, Q18, Q19, Q2, Q20, Q21, Q22, Q23, Q24, Q25, Q26, Q27, Q28, Q29, Q3, Q30, Q31, Q32, Q33, Q34, Q35, Q36, Q37, Q38, Q39, Q4, Q40, Q41, Q42, Q5, Q6, Q7, Q8, Q9: value Q_NMOS_DGS -> 2N7002
- Q43: value Q_NJFET_GSD -> C3M0065090J
- R1, R10, R100, R103, R106, R109, R112, R115, R118, R121, R124, R13, R16, R19, R22, R25, R28, R31, R34, R37, R4, R40, R43, R46, R49, R52, R55, R58, R61, R64, R67, R7, R70, R73, R76, R79, R82, R85, R88, R91, R94, R97: value 0 -> 330
- R101, R104, R107, R11, R110, R113, R116, R119, R122, R125, R14, R17, R2, R20, R23, R26, R29, R32, R35, R38, R41, R44, R47, R5, R50, R53, R56, R59, R62, R65, R68, R71, R74, R77, R8, R80, R83, R86, R89, R92, R95, R98: value 1k -> 4.75k
- R169, R170, R171, R172: value R -> 4.75k
- R178: value R -> 5
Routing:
- net Net-(C6-Pad1): track 17.9 -> 17.1 mm
- net Net-(C5-Pad1): track 17.9 -> 17.1 mm
- net Net-(C42-Pad1): track 17.9 -> 17.1 mm
- net Net-(C4-Pad1): track 17.9 -> 17.1 mm
- net Net-(C38-Pad1): track 17.9 -> 17.1 mm
- net Net-(C37-Pad1): track 17.9 -> 17.1 mm
- net Net-(C3-Pad1): track 17.9 -> 17.1 mm
- net Net-(C27-Pad1): track 17.9 -> 17.1 mm
- net Net-(C26-Pad1): track 17.9 -> 17.1 mm
- net Net-(C25-Pad1): track 17.9 -> 17.1 mm
- net Net-(C24-Pad1): track 17.9 -> 17.1 mm
- net Net-(C23-Pad1): track 17.9 -> 17.1 mm
- net Net-(C22-Pad1): track 17.9 -> 17.1 mm
- net Net-(C2-Pad1): track 17.9 -> 17.1 mm
- net Net-(C1-Pad1): track 17.9 -> 17.1 mm
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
